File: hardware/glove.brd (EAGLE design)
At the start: 63.5 x 38.1 mm, 58 parts, among them J1 MICRO_USB_B_JST_MC5BR3-M404-4S, J2 TC2030-JLINK-NL, U1 BNO055, U2 LP3855EMP-ADJ, U3 NRF51822QF, U4 MCP73831, X3 ABS05-32.768KHZ-9-T

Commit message: Worked on the BOM
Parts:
- removed C25: 100 nF, passives:0402_CAP
- removed C27: 1.0 nF, passives:0402_CAP
- removed C28: 47 nF, passives:0402_CAP
- removed C29: 4.7 uF, passives:0603_CAP
- removed C30: 1.0 uF, passives:0603_CAP
- removed R17, R18: 10 k, passives:0603-RES
- removed U$1: COMMS, QT1070:QT1070
- added C10, C11, C8, C9: 12 pF, passives:0402_CAP
- added U5: LP3855EMP-ADJ, LP3855EMP-ADJ:SOT150P696X180-5N
- C1: value (none) -> 1.0 uF
- C13, C15: device rcl:C0603 -> passives:0603_CAP
- C14: value 100 nF -> 6.8 nF; device rcl:C0603 -> passives:0603_CAP
- C16: value 6.8 nF -> 100 nF; device rcl:C0603 -> passives:0603_CAP
- C17: value 12 pF -> (none); device passives:0402_CAP -> passives:0603_CAP
- C18: value 12 pF -> 4.7 uF; device passives:0402_CAP -> passives:0603_CAP
- C19: value 12 pF -> 8 nF; device passives:0402_CAP -> passives:0603_CAP
- C2: value (none) -> 4.7 uF
- C20: value 12 pF -> 10 uF; device passives:0402_CAP -> passives:0603_CAP
- C21: value 2.2 nF -> 4.7 uF; device passives:0402_CAP -> passives:0603_CAP
- C22: value 1.0 nF -> 10 uF; device passives:0402_CAP -> passives:0603_CAP
- C3: value (none) -> 100 nF; device passives:0603_CAP -> passives:0402_CAP
- C4: value (none) -> 1.0 nF; device passives:0603_CAP -> passives:0402_CAP
- C5: value 8 nF -> 47 nF; device passives:0603_CAP -> passives:0402_CAP
- C6: value 10 uF -> 1.0 nF; device passives:0603_CAP -> passives:0402_CAP
- C7: value 10 uF -> 2.2 nF; device passives:0603_CAP -> passives:0402_CAP
- J1: value MICRO_USB_B_JST_MC5BR3-M404-4S -> TC2030-JLINK-NL; device connector:USB_MICRO_B-JST-MC5BR3-M404-4S-TB -> connector:TC2030-IDC-NL
- J2: value TC2030-JLINK-NL -> MICRO_USB_B_JST_MC5BR3-M404-4S; device connector:TC2030-IDC-NL -> connector:USB_MICRO_B-JST-MC5BR3-M404-4S-TB
- R1, R3: value 10 K -> 1 k; device rcl:R0603 -> passives:0603-RES
- R10, R11, R6: value (none) -> 10 k
- R12: value 440 -> 10 k
- R13: value 250 -> 470
- R14: value 1k -> 250
- R15: value 10 k -> 440
- R16: value 10 k -> 2 k
- R2: value 10 K -> 150; device rcl:R0603 -> passives:0603-RES
- R4: value (none) -> 1 k
- R5: value (none) -> 12 k
- R8: value (none) -> 47 k
- R9: value 47 k -> 10 k
- U1: value BNO055 -> NRF51822QF; device BNO055:LGA28R50P4X10_380X520X100 -> chips:QFN-48-6MM
- U2: value LP3855EMP-ADJ -> BNO055; device LP3855EMP-ADJ:SOT150P696X180-5N -> BNO055:LGA28R50P4X10_380X520X100
- U3: value NRF51822QF -> AT42QT1070; device chips:QFN-48-6MM -> QT1070:QT1070
- moved U3 53.8 mm to (-4.32, -4.57)
- moved C7 48.7 mm to (53.3, 10.7), turned to 270 degrees
- moved C5 48.1 mm to (51.6, 10.7)
- moved R4 48.1 mm to (2.54, -7.11), turned to 0 degrees
- moved C19 47.1 mm to (7.80, 30.7), turned to 270 degrees
- moved R14 45.9 mm to (2.84, 31.3), turned to 0 degrees
- moved C20 43.5 mm to (7.70, 27.6), turned to 90 degrees
- moved C22 40.6 mm to (9.73, 30.7), turned to 270 degrees
- moved C6 40.6 mm to (48.1, 17.5), turned to 90 degrees
- moved R3 40.3 mm to (2.54, -3.81), turned to 0 degrees
- moved C21 36.7 mm to (16.7, 11.0), turned to 0 degrees
- moved R12 35.5 mm to (37.6, 19.6)
- moved J1 35.2 mm to (34.5, 4.57), turned to 180 degrees
- moved J2 35.2 mm to (1.91, 17.8), turned to 270 degrees
- moved R15 35.1 mm to (2.84, 26.9)
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- renumbered C24 to C12, L10 to L2, L9 to L1, X3 to X1
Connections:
- removed net SLCK: U3.15
- removed net VDD: C14.1, C15.1, C16.1, R1.2, R2.2, R3.2, U1.28, U1.3
- net FLEX0: now also U1.5; no longer U3.5
- net FLEX1: now also U1.6; no longer U3.6
- net FLEX2: now also U1.7; no longer U3.7
- net FLEX3: now also U1.8; no longer U3.8
- net GND: now also C10.2, C11.2, C22.1, C5.2, C6.2, C8.2, C9.2, R14.2, R16.1, R2.1, U1.13, U1.33, U1.34, U1.GND, U2.17, U2.6, U3.14, U3.2, U5.5; no longer C19.2, C22.2, C25.2, C27.2, C28.2, C29.2, C30.2, C6.1, R13.2, R4.1, R7.1, U$1.P$14, U$1.P$2, U1.17, U1.5, U1.6, U3.13, U3.33, U3.34, U3.GND
- net GNDIO: now also U2.10, U2.15, U2.16, U2.18, U2.2, U2.25; no longer U1.10, U1.15, U1.16, U1.18, U1.2, U1.25
- net INT: now also U2.14; no longer U1.14
- net N$1: now also C21.1; no longer C2.1, C3.1
- net N$14: now also U1.2; no longer U3.2
- net N$16: now also C1.1, C4.1, U1.35, U1.36; no longer C27.1, C30.1, U3.35, U3.36
- net N$17: now also R8.1, U3.5; no longer R9.1, U$1.P$5
- net N$18: now also R6.1, U2.4; no longer R3.1, U1.4
- net N$19: now also J1.2, R2.2, U1.23; no longer J2.2, R4.2, U3.23
- net N$2: now also LED2.A, R13.1; no longer LED1.A, R6.1
- net N$20: now also C11.1, U1.38; no longer C20.1, U3.38
- net N$21: now also U1.31; no longer U3.31
- net N$22: now also U1.32; no longer U3.32
- net N$23: now also C7.1, U1.30; no longer C21.1, U3.30
- net N$25: now also C5.1, U1.29; no longer C28.1, U3.29
- net N$26: now also C6.1, U1.39; no longer C22.1, U3.39
- net N$27: now also C8.1, U1.45; no longer C17.1, U3.45
- net N$28: now also C9.1, U1.46; no longer C18.1, U3.46
- net N$29: now also C10.1, U1.37; no longer C19.1, U3.37
- net N$3: now also LED2.C; no longer LED1.C
- net N$30: now also J1.4, U1.24; no longer J2.4, U3.24
- net N$31: now also R11.2, U3.10; no longer R15.2, U$1.P$10
- net N$32: now also R11.1; no longer R15.1
- net N$33: now also R9.2, U3.11; no longer R16.2, U$1.P$11
- net N$34: now also R9.1; no longer R16.1
- net N$35: now also R12.2, U3.12; no longer R17.2, U$1.P$12
- net N$36: now also R12.1; no longer R17.1
- net N$37: now also R10.2, U3.13; no longer R18.2, U$1.P$13
- net N$38: now also C18.1, J2.1, R13.2; no longer C1.1, J1.1, R6.2
- net N$39: now also R10.1; no longer R18.1
- net N$4: now also R16.2; no longer R7.2
- net N$40: now also R7.1, U3.4; no longer R8.1, U$1.P$4
- net N$5: now also C22.2, U5.2; no longer C6.2, U2.2
- net N$6: now also LED1.C, U1.19; no longer LED2.C, U3.19
- net N$7: now also C19.1, R14.1, R15.2, U5.4; no longer C5.1, R12.2, R13.1, U2.4
- net N$8: now also LED1.A, R1.1; no longer LED2.A, R14.1
- net N$9: now also U2.9; no longer U1.9
- net SCL: now also R3.1, U1.11, U2.19, U3.6; no longer R1.1, R11.1, U$1.P$6, U1.19, U3.11
- net SDA: now also R4.1, U1.14, U2.20, U3.3; no longer R10.1, R2.1, U$1.P$3, U1.20, U3.14
- net VCC: now also C14.1, C15.1, C16.1, C17.1, C19.2, C2.1, C20.1, C3.1, J1.1, R1.2, R15.1, R3.2, R4.2, R6.2, R7.2, U1.1, U1.12, U2.28, U5.3; no longer C25.1, C29.1, C4.1, C5.2, C7.1, J2.1, R10.2, R11.2, R12.1, R14.2, R9.2, U$1.P$1, U3.12
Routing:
- net VDD: track 50.6 -> 0.00 mm, vias 4 -> 0
- net SDA: track 51.8 -> 4.40 mm, vias 4 -> 2
- net SCL: track 40.5 -> 1.93 mm, vias 3 -> 0
- net VCC: track 82.4 -> 97.8 mm, vias 4 -> 6
- net N$40: track 9.74 -> 1.60 mm
- net N$18: track 18.0 -> 9.91 mm
- net N$17: track 3.79 -> 0.00 mm
- net N$38: track 7.44 -> 4.46 mm
- net N$37: track 2.02 -> 0.00 mm
- net N$35: track 2.02 -> 0.00 mm
- net N$33: track 2.02 -> 0.00 mm
- net N$31: track 2.02 -> 0.00 mm
- net N$1: track 34.8 -> 33.3 mm

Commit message: Started work on BOM
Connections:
- net N$5: now also U5.1
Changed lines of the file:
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@@
 <via x="9.652" y="8.382" extent="1-16" drill="0.6"/>
 <wire x1="9.652" y1="8.382" x2="9.652" y2="28.448" width="0.4064" layer="16"/>
+<contactref element="U5" pad="1"/>
+<wire x1="12.9794" y1="28.448" x2="12.9794" y2="29.9466" width="0" layer="19" extent="1-1"/>
 </signal>
 <signal name="N$7">

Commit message: It's a board
We got this
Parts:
- removed LED1, LED2: LED0603, leds:LED-0603
- added CHG, LED12, LED13, LED14, LED15: LED0603, leds:LED-0603
- added D1, D10, D11, D12, D2, D3, D4, D5, D6, D7, D8, D9: 1N4004, diode:DO41-10
- added PAD1, PAD10, PAD11, PAD12, PAD13, PAD14, PAD15, PAD2, PAD3, PAD4, PAD5, PAD6, PAD7, PAD8, PAD9: WIREPAD1,6/0,8, wirepad:1,6/0,8
- added R17, R18, R19: 1 k, passives:0603-RES
- added R20, R21, R22, R23: (no value), passives:0603-RES
- moved U3 55.0 mm to (44.5, 20.9), turned to 90 degrees
- moved R6 40.9 mm to (12.7, 29.2), turned to 270 degrees
- moved R4 35.9 mm to (33.3, 11.4), turned to 90 degrees
- moved C19 34.2 mm to (36.8, 12.7), turned to 0 degrees
- moved C20 33.9 mm to (36.8, 10.2), turned to 0 degrees
- moved A1 33.7 mm to (26.7, 29.8), turned to 180 degrees
- moved R3 32.8 mm to (31.6, 11.4), turned to 90 degrees
- moved C16 29.9 mm to (21.6, 8.89), turned to 0 degrees
- moved U2 29.8 mm to (2.51, 28.7)
- moved X2 29.0 mm to (22.2, 14.8), turned to 180 degrees
- moved C11 28.4 mm to (22.9, 16.5)
- moved C10 28.4 mm to (25.4, 16.5), turned to 0 degrees
- moved B1 26.9 mm to (29.2, 25.4), turned to 90 degrees
- moved C8 26.1 mm to (21.8, 12.1), turned to 0 degrees
- moved C6 23.5 mm to (24.9, 14.1), turned to 180 degrees
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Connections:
- new net HEART: PAD3.1, U1.9
- new net N$10: LED15.C, U1.21
- new net N$11: LED15.A, R17.1
- new net N$12: LED12.C, U1.18
- new net N$13: LED12.A, R18.1
- new net N$41: D4.C, PAD6.1
- new net N$42: LED13.A, R19.1
- new net N$43: LED13.C, U1.19
- new net N$44: D1.C, PAD4.1
- new net N$45: D2.A, PAD5.1
- new net N$46: D2.C, D3.A
- new net N$47: D5.A, PAD7.1
- new net N$48: D5.C, D6.A
- new net N$49: D7.C, PAD8.1
- new net N$50: D8.A, PAD9.1
- new net N$51: D8.C, D9.A
- new net N$52: D10.C, PAD10.1
- new net N$53: D11.A, PAD11.1
- new net N$54: D11.C, D12.A
- net FLEX0: now also D3.C, R20.1
- net FLEX1: now also D6.C, R21.1
- net FLEX2: now also D9.C, R22.1
- net FLEX3: now also D12.C, R23.1
- net GND: now also PAD2.1, R20.2, R21.2, R22.2, R23.2
- net N$2: now also CHG.A; no longer LED2.A
- net N$3: now also CHG.C; no longer LED2.C
- net N$32: now also PAD12.1
- net N$34: now also PAD13.1
- net N$36: now also PAD14.1
- net N$39: now also PAD15.1
- net N$6: now also LED14.C, U1.20; no longer LED1.C, U1.19
- net N$8: now also LED14.A; no longer LED1.A
- net VCC: now also D1.A, D10.A, D4.A, D7.A, PAD1.1, R17.2, R18.2, R19.2
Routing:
- net VCC: track 97.8 -> 0.00 mm, vias 6 -> 0
- net GNDIO: track 46.2 -> 0.00 mm
- net GND: track 38.0 -> 0.00 mm, vias 22 -> 0
- net N$5: track 33.9 -> 0.00 mm, vias 2 -> 0
- net N$1: track 33.3 -> 0.00 mm
- net N$16: track 29.2 -> 0.00 mm, vias 2 -> 0
- net N$30: track 26.0 -> 0.00 mm
- net N$7: track 22.7 -> 0.00 mm
- net N$9: track 20.8 -> 0.00 mm
- net N$19: track 17.0 -> 0.00 mm
- net N$3: track 10.4 -> 0.00 mm, vias 2 -> 0
- net N$18: track 9.91 -> 0.00 mm
- net N$20: track 7.16 -> 0.00 mm
- net N$29: track 7.08 -> 0.00 mm
- net N$28: track 7.01 -> 0.00 mm
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- removed copper zone on layer 16, net GND
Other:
- board size 63.5 x 38.1 mm -> 50.8 x 31.8 mm

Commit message: lol haf done boardl
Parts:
- removed D1, D10, D11, D12, D2, D3, D4, D5, D6, D7, D8, D9: 1N4004, diode:DO41-10
- added C23: 1uF, passives:0603_CAP
- added R24: 100k, passives:0603-RES
- moved C20 32.2 mm to (6.65, 21.5), turned to 90 degrees
- moved C19 28.9 mm to (8.94, 20.1), turned to 180 degrees
- moved R7 21.6 mm to (36.4, 24.8)
- moved R8 20.4 mm to (38.7, 21.2)
- moved R21 18.1 mm to (26.0, 6.58)
- moved C18 16.3 mm to (9.91, 16.7), turned to 270 degrees
- moved C22 13.3 mm to (8.76, 23.6), turned to 180 degrees
- moved C15 12.8 mm to (5.87, 27.6)
- moved C17 8.98 mm to (24.1, 22.9)
- moved R3 8.78 mm to (40.0, 13.7), turned to 180 degrees
- moved CHG 7.68 mm to (14.7, 16.4)
- moved R4 7.67 mm to (40.0, 15.2), turned to 180 degrees
- moved C16 6.48 mm to (20.3, 2.54), turned to 90 degrees
- moved C12 6.19 mm to (26.8, 26.5), turned to 180 degrees
- moved R17 6.13 mm to (42.4, 7.01)
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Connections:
- removed net N$44: D1.C, PAD4.1
- removed net N$45: D2.A, PAD5.1
- removed net N$46: D2.C, D3.A
- removed net N$47: D5.A, PAD7.1
- removed net N$48: D5.C, D6.A
- removed net N$49: D7.C, PAD8.1
- removed net N$50: D8.A, PAD9.1
- removed net N$51: D8.C, D9.A
- removed net N$52: D10.C, PAD10.1
- removed net N$53: D11.A, PAD11.1
- removed net N$54: D11.C, D12.A
- net FLEX0: now also PAD5.1; no longer D3.C
- net FLEX1: now also PAD7.1; no longer D6.C
- net FLEX2: now also PAD9.1; no longer D9.C
- net FLEX3: now also PAD11.1; no longer D12.C
- net GND: now also C23.1, R24.1
- net N$1: no longer SW1.P1, SW1.P2
- net N$38: now also R24.2
- net N$41: now also C23.2, SW1.P1, SW1.P2; no longer D4.C, PAD6.1
- net VCC: now also PAD10.1, PAD4.1, PAD6.1, PAD8.1; no longer D1.A, D10.A, D4.A, D7.A
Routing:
- net VCC: track 0.00 -> 52.9 mm, vias 0 -> 2
- net N$5: track 0.00 -> 31.7 mm, vias 0 -> 2
- net GND: track 0.00 -> 16.7 mm, vias 0 -> 1
- net FLEX0: track 0.00 -> 16.5 mm
- net FLEX1: track 0.00 -> 14.9 mm
- net FLEX2: track 0.00 -> 13.7 mm
- net HEART: track 0.00 -> 13.7 mm
- net GNDIO: track 0.00 -> 13.2 mm
- net N$16: track 0.00 -> 13.2 mm, vias 0 -> 2
- net FLEX3: track 0.00 -> 12.3 mm
- net N$1: track 0.00 -> 10.6 mm
- net SCL: track 0.00 -> 10.3 mm
- net N$38: track 0.00 -> 8.54 mm
- net N$9: track 0.00 -> 8.34 mm, vias 0 -> 2
- net N$23: track 0.00 -> 7.24 mm
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- added copper zone on layer 16, net GND

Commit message: 54 wires left! (woo?)
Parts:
- added D1: B130LAW, load_balance:2PIN
- added P1: DMP1045U, load_balance:3PIN
- PAD1, PAD10, PAD11, PAD2, PAD3, PAD4, PAD5, PAD6, PAD7, PAD8, PAD9: value WIREPAD1,6/0,8 -> WIREPAD1,6/0,9; device wirepad:1,6/0,8 -> wirepad:1,6/0,9
- moved R24 18.2 mm to (6.35, 8.89), turned to 90 degrees
- moved C23 17.0 mm to (10.2, 10.2)
- moved C5 14.2 mm to (24.0, 25.2), turned to 180 degrees
- moved LED15 8.13 mm to (41.0, 8.64)
- moved LED13 8.03 mm to (33.6, 4.80)
- moved R2 6.48 mm to (47.0, 10.9)
- moved LED14 6.35 mm to (39.9, 5.03)
- moved R19 5.89 mm to (33.6, 6.48), turned to 180 degrees
- moved LED12 5.68 mm to (36.2, 7.57)
- moved SW1 5.45 mm to (5.56, -0.08)
- moved C21 5.29 mm to (11.8, 4.45)
- moved CN1 5.20 mm to (15.6, -1.60)
- moved J1 5.08 mm to (45.8, 4.52)
- moved PAD1 5.08 mm to (34.3, -3.48)
- moved PAD10 5.08 mm to (30.5, -3.48)
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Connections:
- net N$1: now also C23.2, D1.OUT, P1.3, SW1.P1, SW1.P2; no longer C21.1, CN1.1, U4.3
- net N$38: now also D1.IN, P1.2
- net N$41: now also C21.1, CN1.1, P1.1, U4.3; no longer C23.2, SW1.P1, SW1.P2
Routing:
- net N$38: track 8.54 -> 31.7 mm, vias 0 -> 2
- net N$1: track 10.6 -> 23.4 mm
- net N$25: track 0.00 -> 12.4 mm, vias 0 -> 2
- net N$41: track 5.60 -> 14.5 mm
- net HEART: track 13.7 -> 18.8 mm
- net FLEX2: track 13.7 -> 18.8 mm
- net FLEX3: track 12.3 -> 17.4 mm
- net FLEX1: track 14.9 -> 19.5 mm
- net FLEX0: track 16.5 -> 21.1 mm
- net N$5: track 31.7 -> 35.1 mm
- net N$16: track 13.2 -> 16.3 mm
- net VCC: track 52.9 -> 54.8 mm
- net N$23: track 7.24 -> 8.89 mm
- net GNDIO: track 13.2 -> 14.1 mm
- net GND: vias 1 -> 2
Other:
- board size 50.8 x 31.8 mm -> 50.8 x 36.8 mm

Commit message: Did a few more easy wires. 44 left!
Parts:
- moved C16 6.38 mm to (20.7, 4.70)
- moved R18 3.13 mm to (33.2, 10.8)
- moved LED12 2.41 mm to (34.6, 9.37), turned to 270 degrees
- moved R1 1.88 mm to (41.4, 7.87), turned to 0 degrees
- moved LED13 1.82 mm to (34.6, 6.32), turned to 270 degrees
- moved R19 1.55 mm to (33.2, 7.98)
- moved LED14 1.51 mm to (40.0, 6.53)
- moved R17 1.40 mm to (40.5, 10.8)
- moved LED15 1.30 mm to (39.9, 9.37)
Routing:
- net VCC: track 54.8 -> 85.9 mm
- net N$40: track 0.00 -> 13.6 mm, vias 0 -> 2
- net N$17: track 0.00 -> 9.37 mm, vias 0 -> 2
- net N$11: track 0.00 -> 1.77 mm
- net N$42: track 0.00 -> 1.65 mm
- net N$13: track 0.00 -> 1.47 mm
- net N$8: track 0.00 -> 1.35 mm

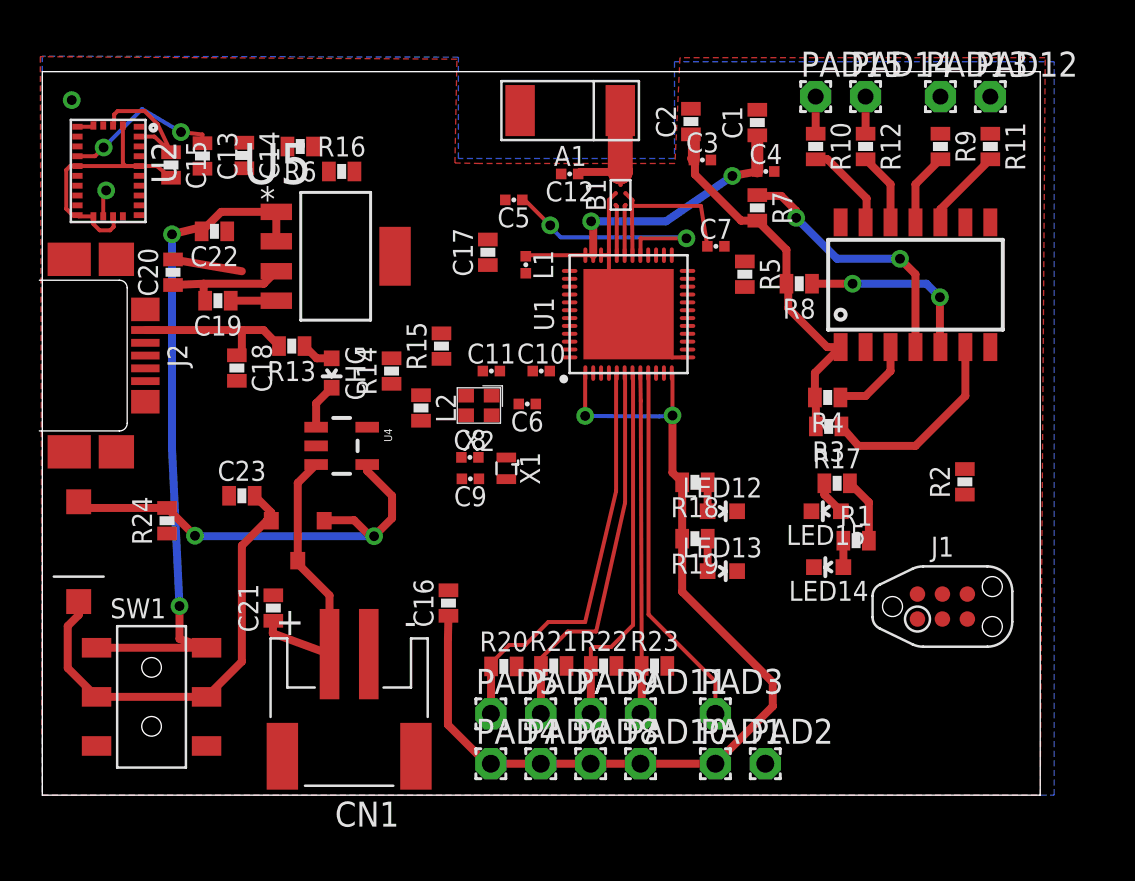
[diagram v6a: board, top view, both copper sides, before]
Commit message: Completely routed!
Some final layout tweaks needed, but everything is connected and it looks like it works
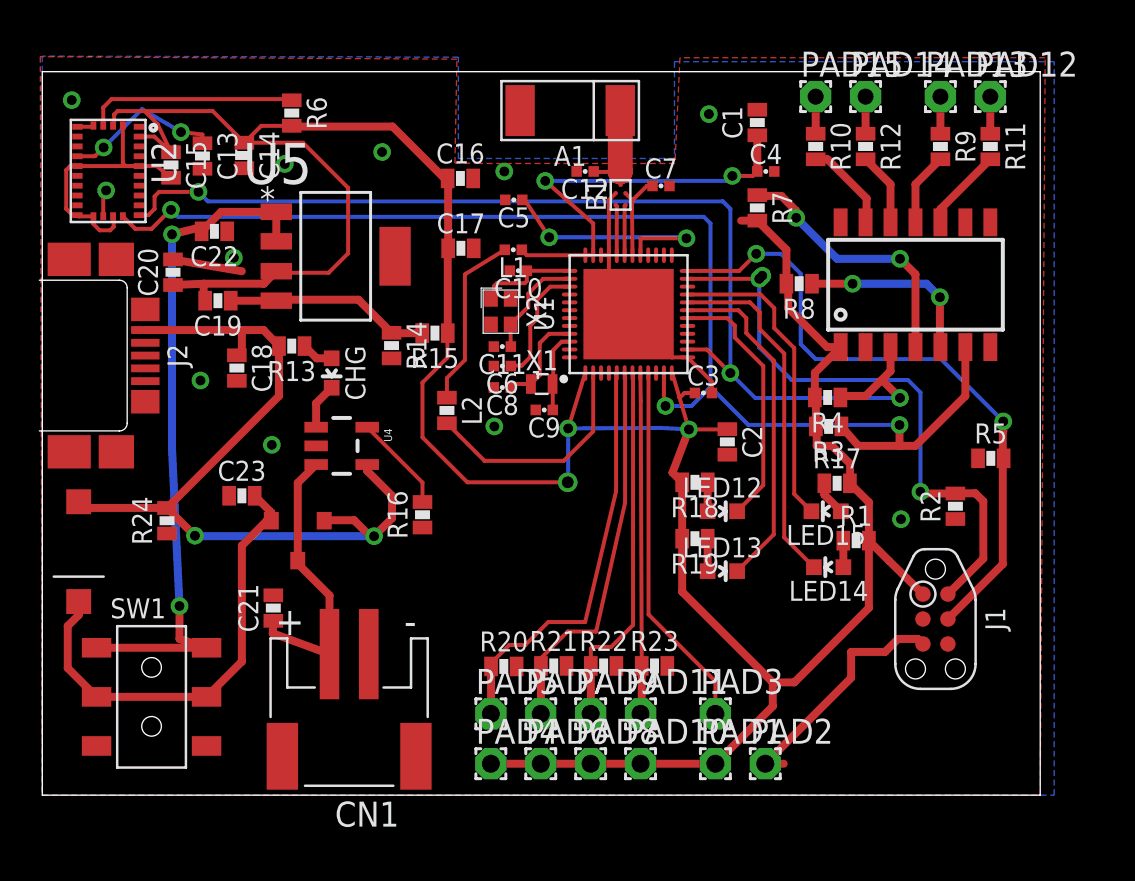
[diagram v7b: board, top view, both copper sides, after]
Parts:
- moved C16 21.6 mm to (21.3, 26.3), turned to 0 degrees
- moved R16 18.0 mm to (19.4, 9.19), turned to 90 degrees
- moved C2 16.4 mm to (34.9, 12.9), turned to 270 degrees
- moved R5 15.6 mm to (48.3, 12.1), turned to 0 degrees
- moved C3 11.9 mm to (33.7, 15.4)
- moved C10 5.24 mm to (24.2, 21.6), turned to 180 degrees
- moved C9 5.14 mm to (25.6, 14.5)
- moved X2 4.90 mm to (23.3, 19.5), turned to 270 degrees
- moved X1 4.66 mm to (25.4, 15.8), turned to 0 degrees
- moved C7 4.15 mm to (31.5, 25.9)
- moved C8 3.92 mm to (23.4, 15.7), turned to 180 degrees
- moved C6 2.31 mm to (23.4, 16.8)
- moved R6 1.76 mm to (12.7, 29.6), turned to 270 degrees
- moved C17 1.39 mm to (21.3, 22.8), turned to 0 degrees
- moved C11 1.36 mm to (23.4, 17.8), turned to 180 degrees
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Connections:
- removed net GNDIO: C13.2, C14.2, C15.2, C16.2, U2.10, U2.15, U2.16, U2.18, U2.2, U2.25
- net GND: now also C13.2, C14.2, C15.2, C16.2, U2.10, U2.15, U2.16, U2.18, U2.2, U2.25
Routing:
- net VCC: track 85.9 -> 151.4 mm, vias 2 -> 3
- net SCL: track 10.3 -> 65.4 mm, vias 0 -> 3
- net SDA: track 4.33 -> 57.2 mm, vias 0 -> 3
- net N$30: track 0.00 -> 33.4 mm, vias 0 -> 2
- net N$19: track 0.00 -> 30.5 mm, vias 0 -> 3
- net GND: track 16.7 -> 45.6 mm, vias 2 -> 11
- net N$6: track 0.00 -> 18.0 mm
- net N$43: track 0.00 -> 17.4 mm
- net N$10: track 0.00 -> 15.8 mm
- net GNDIO: track 14.1 -> 0.00 mm
- net N$12: track 0.00 -> 13.2 mm
- net N$14: track 0.00 -> 11.8 mm
- net N$18: track 0.00 -> 10.7 mm
- net N$38: track 31.7 -> 42.3 mm
- net N$15: track 0.00 -> 9.03 mm
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
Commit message: Need to finish silkscreen
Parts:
- C17: value (none) -> 100 nF
- R7: value (none) -> 47 k
- moved R8 0.73 mm to (38.2, 20.3), turned to 270 degrees
- moved C20 0.07 mm to (6.60, 21.6)
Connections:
- removed net INT: U2.14
- removed net N$17: R8.1, U3.5
- new net !CHANGE: R8.1, U1.22, U3.5
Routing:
- net !CHANGE: track 0.00 -> 15.8 mm, vias 0 -> 2
- net N$17: track 9.37 -> 0.00 mm, vias 2 -> 0
- net VCC: track 151.4 -> 154.9 mm
- net N$38: track 42.3 -> 40.6 mm
- net FLEX0: track 21.1 -> 20.0 mm
- net N$9: track 8.13 -> 7.32 mm
- net N$19: track 30.5 -> 31.2 mm, vias 3 -> 2
- net FLEX2: track 18.8 -> 18.2 mm
